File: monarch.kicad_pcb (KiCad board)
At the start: 2 copper layers, 159.6 x 123.3 mm, 141 parts, among them J1 USB_C_Receptacle_USB2.0, J2 USB_C_Receptacle_USB2.0, J3 OLED, SW1 SW_PUSH, SW10 SW_PUSH, SW11 SW_PUSH, SW12 SW_PUSH, SW13 SW_PUSH, SW14 SW_PUSH, SW15 SW_PUSH, SW16 SW_PUSH, SW17 SW_PUSH, SW18 SW_PUSH, SW19 Rotary_Encoder, SW2 SW_PUSH, SW20 SW_PUSH, SW21 SW_PUSH, SW22 SW_PUSH, SW23 SW_PUSH, SW24 SW_PUSH, SW3 SW_PUSH, SW4 SW_PUSH, SW5 SW_PUSH, SW6 SW_PUSH, SW7 SW_PUSH, SW8 SW_PUSH, SW9 SW_PUSH, U1 ATMEGA32U4, U2 MIC5219-5.0YMM, X1 16Mhz

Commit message: start routing
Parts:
- removed R10, R9: 330, Resistor_SMD:R_0805_2012Metric
- removed R11, R12: 5.1k, Resistor_SMD:R_0805_2012Metric
- J1, J2: footprint private:USB_C_TH_6pin -> Connector_USB:USB_C_Receptacle_GCT_USB4085; moved to B.Cu
- L1, L2: moved to F.Cu
- moved L1 169.7 mm to (181.0, 86.5), turned to 80 degrees
- moved L2 151.8 mm to (171.1, 84.1), turned to 80 degrees
- moved L34 143.7 mm to (18.3, 72.0)
- moved C3 139.2 mm to (21.0, 30.0)
- moved JP1 132.7 mm to (32.9, 22.6)
- moved L35 120.1 mm to (19.1, 30.6)
- moved L3 110.5 mm to (138.7, 18.9)
- moved L33 109.5 mm to (59.3, 96.0)
- moved R4 109.4 mm to (39.0, 14.7), turned to 0 degrees
- moved R3 108.5 mm to (39.0, 12.6), turned to 0 degrees
- moved R1 96.4 mm to (144.2, 19.6)
- moved L15 95.3 mm to (119.2, 49.0), turned to 0 degrees
- moved L20 95.3 mm to (24.2, 56.8), turned to 0 degrees
- moved L4 80.1 mm to (155.2, 46.1)
- moved L8 64.8 mm to (119.4, 117.2)
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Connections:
- R3 pad 1: +5V -> GND
- R4 pad 1: +5V -> GND
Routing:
- net VCC: track 0.00 -> 468.2 mm, vias 0 -> 2
- net A5: track 0.00 -> 185.9 mm
- net A2: track 0.00 -> 129.7 mm
- net A1: track 0.00 -> 113.2 mm
- net A3: track 0.00 -> 110.8 mm
- net A4: track 0.00 -> 109.1 mm, vias 0 -> 2
- net A0: track 0.00 -> 99.9 mm
- net Net-(BZ1-Pad1): track 0.00 -> 88.3 mm, vias 0 -> 2
- net Net-(L33-Pad3): track 0.00 -> 72.7 mm
- net Net-(L33-Pad1): track 0.00 -> 53.5 mm, vias 0 -> 2
- net COL0: track 38.4 -> 91.7 mm
- net Net-(L34-Pad1): track 0.00 -> 47.4 mm
- net Net-(D27-Pad1): track 0.00 -> 47.4 mm
- net COL1: track 38.0 -> 85.0 mm, vias 0 -> 4
- net RX: track 0.00 -> 39.4 mm
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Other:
- net class Default: via_dia 0.8 -> 0.6; via_drill 0.4 -> 0.3

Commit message: plate edge case
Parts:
- removed the H9 at (165.0, 126.7)
- removed the H9 at (147.8, 91.7)
- added H1: Hole, MountingHole:MountingHole_2.2mm_M2, F.Cu at (132.0, 14.2)
- added H1: Hole, MountingHole:MountingHole_2.2mm_M2, F.Cu at (155.6, 20.4)
- added H1: Hole, MountingHole:MountingHole_2.2mm_M2, F.Cu at (111.0, 120.7)
- added H1: Hole, MountingHole:MountingHole_2.2mm_M2, F.Cu at (14.9, 90.9)
- added H1: Hole, MountingHole:MountingHole_2.2mm_M2, F.Cu at (15.6, 15.1)
- added H1: Hole, MountingHole:MountingHole_2.2mm_M2, F.Cu at (77.8, 8.11)
- added H9: Hole, MountingHole:MountingHole_2.2mm_M2, F.Cu at (167.4, 130.7)
- moved L1 103.0 mm to (78.6, 75.6), turned to 0 degrees
- moved L2 84.9 mm to (86.7, 75.7), turned to 0 degrees
- moved R3 15.6 mm to (26.5, 21.9), turned to 90 degrees
- moved H10 12.4 mm to (81.2, 102.2)
- moved R4 5.89 mm to (33.4, 13.1), turned to 270 degrees
- moved L7 4.63 mm to (154.4, 121.6), turned to 350 degrees
- moved RED1 3.13 mm to (149.6, 23.4)
- moved L3 2.41 mm to (138.9, 16.6)
- moved L8 2.20 mm to (120.7, 115.4), turned to 350 degrees
- moved L43 2.00 mm to (122.0, 19.5)
- moved D26 1.88 mm to (134.6, 23.4)
- moved J2 1.07 mm to (163.5, 97.5)
- moved L42 1.00 mm to (109.8, 16.5)
- moved H2 0.94 mm to (155.6, 86.2)
- moved H4 0.60 mm to (132.0, 82.2)
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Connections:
- D1 pad 1: A3 -> A2
- D10 pad 1: A2 -> A3
- D11 pad 1: A2 -> A3
- D12 pad 1: A2 -> A3
- D2 pad 1: A3 -> A2
- D3 pad 1: A3 -> A2
- D4 pad 1: A3 -> A2
- D5 pad 1: A3 -> A2
- D6 pad 1: A3 -> A2
- D7 pad 1: A2 -> A3
- D8 pad 1: A2 -> A3
- D9 pad 1: A2 -> A3
- J2 pad A5: +5V -> GND
- J2 pad B5: +5V -> GND
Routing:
- net A5: track 185.9 -> 0.00 mm
- net Net-(J1-PadA6): track 0.00 -> 147.7 mm, vias 0 -> 1
- net Net-(J1-PadA7): track 0.00 -> 142.3 mm, vias 0 -> 1
- net COL2: track 95.3 -> 229.6 mm, vias 6 -> 9
- net COL0: track 91.7 -> 196.7 mm, vias 0 -> 3
- net VCC: track 468.2 -> 372.8 mm
- net COL1: track 85.0 -> 169.1 mm, vias 4 -> 7
- net Net-(L33-Pad3): track 72.7 -> 0.00 mm
- net COL4: track 103.7 -> 172.4 mm, vias 4 -> 5
- net Net-(L7-Pad1): track 38.6 -> 0.00 mm
- net Net-(L3-Pad1): track 34.9 -> 0.00 mm
- net GND: track 0.00 -> 22.1 mm
- net Net-(L6-Pad1): track 21.5 -> 0.00 mm
- net A1: track 113.2 -> 133.0 mm, vias 0 -> 2
- net A3: track 110.8 -> 129.4 mm, vias 0 -> 2
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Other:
- board size 159.6 x 123.3 mm -> 165.4 x 129.6 mm

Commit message: routing almost complete
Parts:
- moved L1 73.2 mm to (117.2, 13.4)
- moved L2 73.2 mm to (125.3, 13.5)
- moved R8 26.1 mm to (156.7, 64.5)
- moved R7 2.90 mm to (131.5, 67.9)
- moved C5 2.30 mm to (131.5, 71.5)
- moved R5 1.70 mm to (131.5, 65.4)
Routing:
- net VCC: track 372.8 -> 934.1 mm, vias 2 -> 6
- net UVCC: track 29.6 -> 193.7 mm, vias 0 -> 2
- net D10: track 0.00 -> 160.3 mm, vias 0 -> 1
- net COL3: track 38.0 -> 180.8 mm, vias 4 -> 5
- net A5: track 0.00 -> 105.3 mm, vias 0 -> 2
- net Net-(D26-Pad1): track 0.00 -> 70.1 mm
- net Net-(L33-Pad3): track 0.00 -> 66.6 mm
- net A0: track 101.6 -> 161.3 mm, vias 2 -> 4
- net GND: track 22.1 -> 76.8 mm, vias 3 -> 21
- net COL2: track 229.6 -> 176.2 mm
- net Net-(L26-Pad1): track 0.00 -> 51.9 mm, vias 0 -> 2
- net D2: track 0.00 -> 51.1 mm, vias 0 -> 1
- net D3: track 0.00 -> 49.3 mm, vias 0 -> 1
- net Net-(L3-Pad1): track 0.00 -> 42.6 mm
- net Net-(L7-Pad1): track 0.00 -> 31.8 mm
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
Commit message: rerouting v2
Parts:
- X1: footprint Crystal:Crystal_SMD_SeikoEpson_FA238-4Pin_3.2x2.5mm -> Crystal:Crystal_SMD_7050-4Pin_7.0x5.0mm
- moved R6 44.6 mm to (148.1, 18.0), turned to 180 degrees
- moved R3 8.26 mm to (23.9, 14.1), turned to 270 degrees
- moved R4 7.00 mm to (26.4, 14.0)
- moved C4 2.25 mm to (147.7, 79.2), turned to 135 degrees
- moved C2 1.53 mm to (155.5, 71.3), turned to 135 degrees
- moved X1 0.58 mm to (151.7, 75.3), turned to 45 degrees
- moved L1 0.29 mm to (117.2, 13.2)
- moved L2 0.29 mm to (125.3, 13.2)
- moved J2 0.05 mm to (163.4, 97.5)
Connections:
- X1 pad 3: (no net) -> GND
- X1 pad 4: (no net) -> GND
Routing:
- net GND: track 76.8 -> 153.7 mm, vias 21 -> 22
- net D9: track 0.00 -> 62.3 mm
- net VCC: track 934.1 -> 994.2 mm, vias 6 -> 21
- net Net-(R6-Pad1): track 4.15 -> 51.9 mm, vias 0 -> 2
- net COL4: track 174.8 -> 219.9 mm, vias 5 -> 13
- net Net-(D27-Pad1): track 48.0 -> 11.9 mm
- net A1: track 163.2 -> 130.9 mm, vias 4 -> 2
- net Net-(Boot1-Pad1): track 0.00 -> 29.3 mm, vias 0 -> 2
- net COL1: track 179.1 -> 206.6 mm, vias 7 -> 13
- net COL0: track 199.2 -> 225.6 mm, vias 0 -> 4
- net A4: track 103.9 -> 126.5 mm, vias 2 -> 4
- net COL2: track 176.2 -> 198.7 mm
- net Net-(L2-Pad1): track 0.00 -> 20.0 mm, vias 0 -> 1
- net Net-(D26-Pad1): track 70.1 -> 50.9 mm, vias 0 -> 1
- net A0: track 161.3 -> 142.7 mm, vias 4 -> 0
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
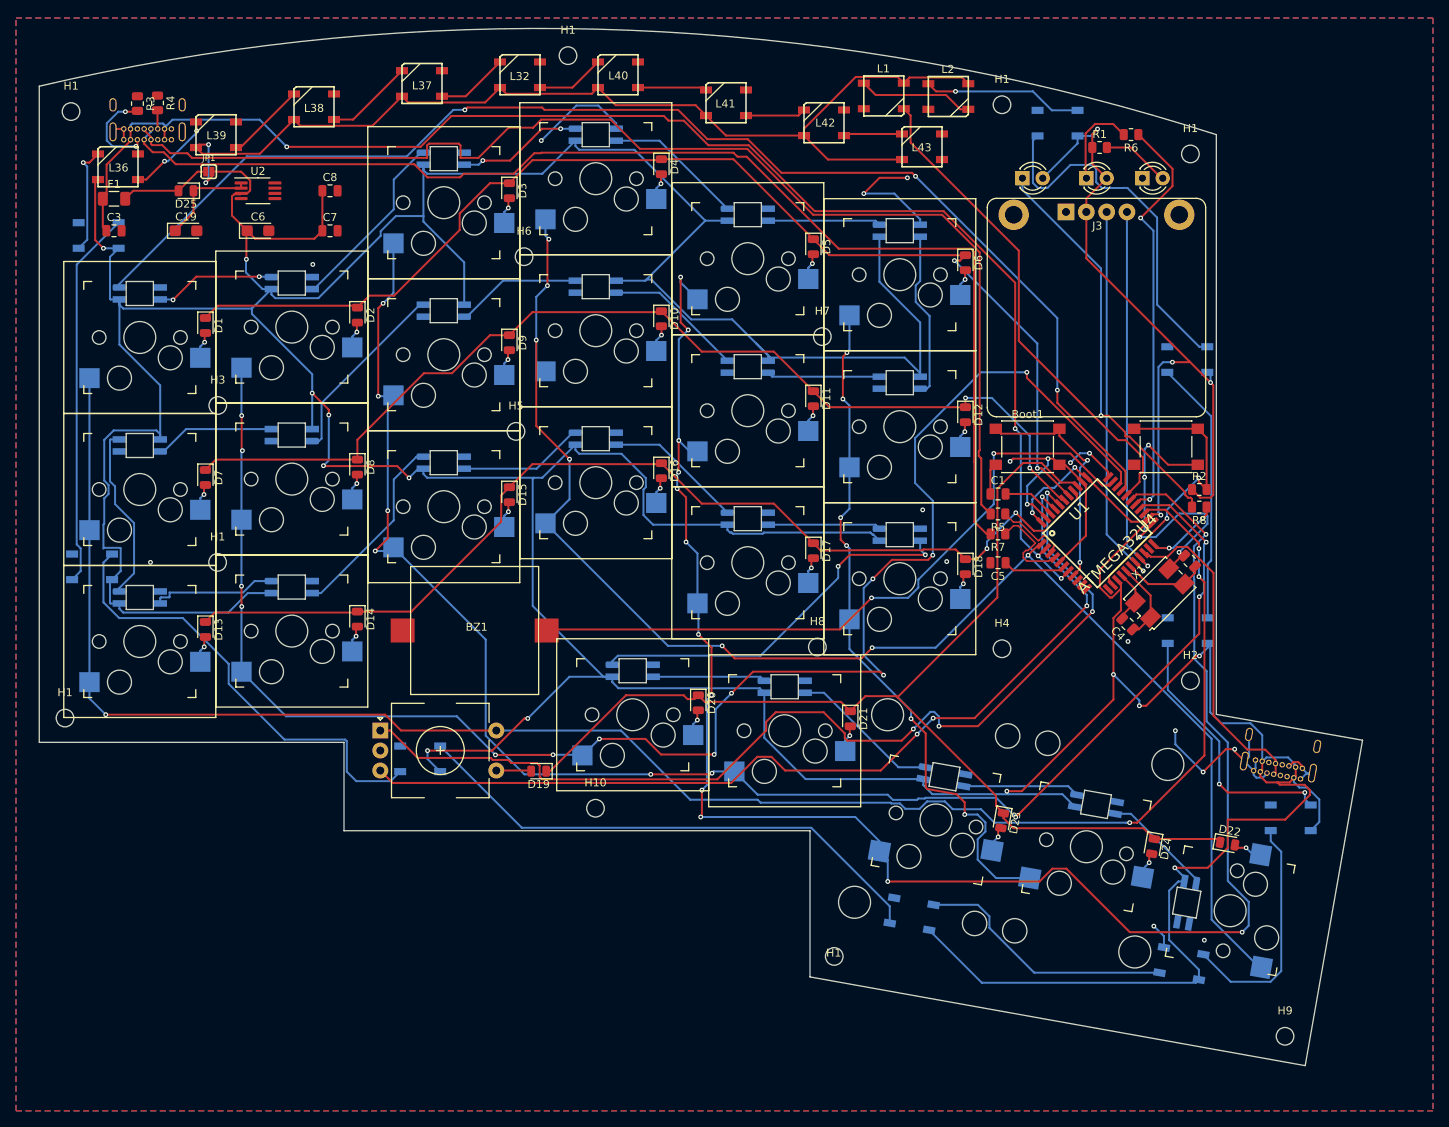
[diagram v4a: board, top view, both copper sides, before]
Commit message: rerouting 0 unrouted
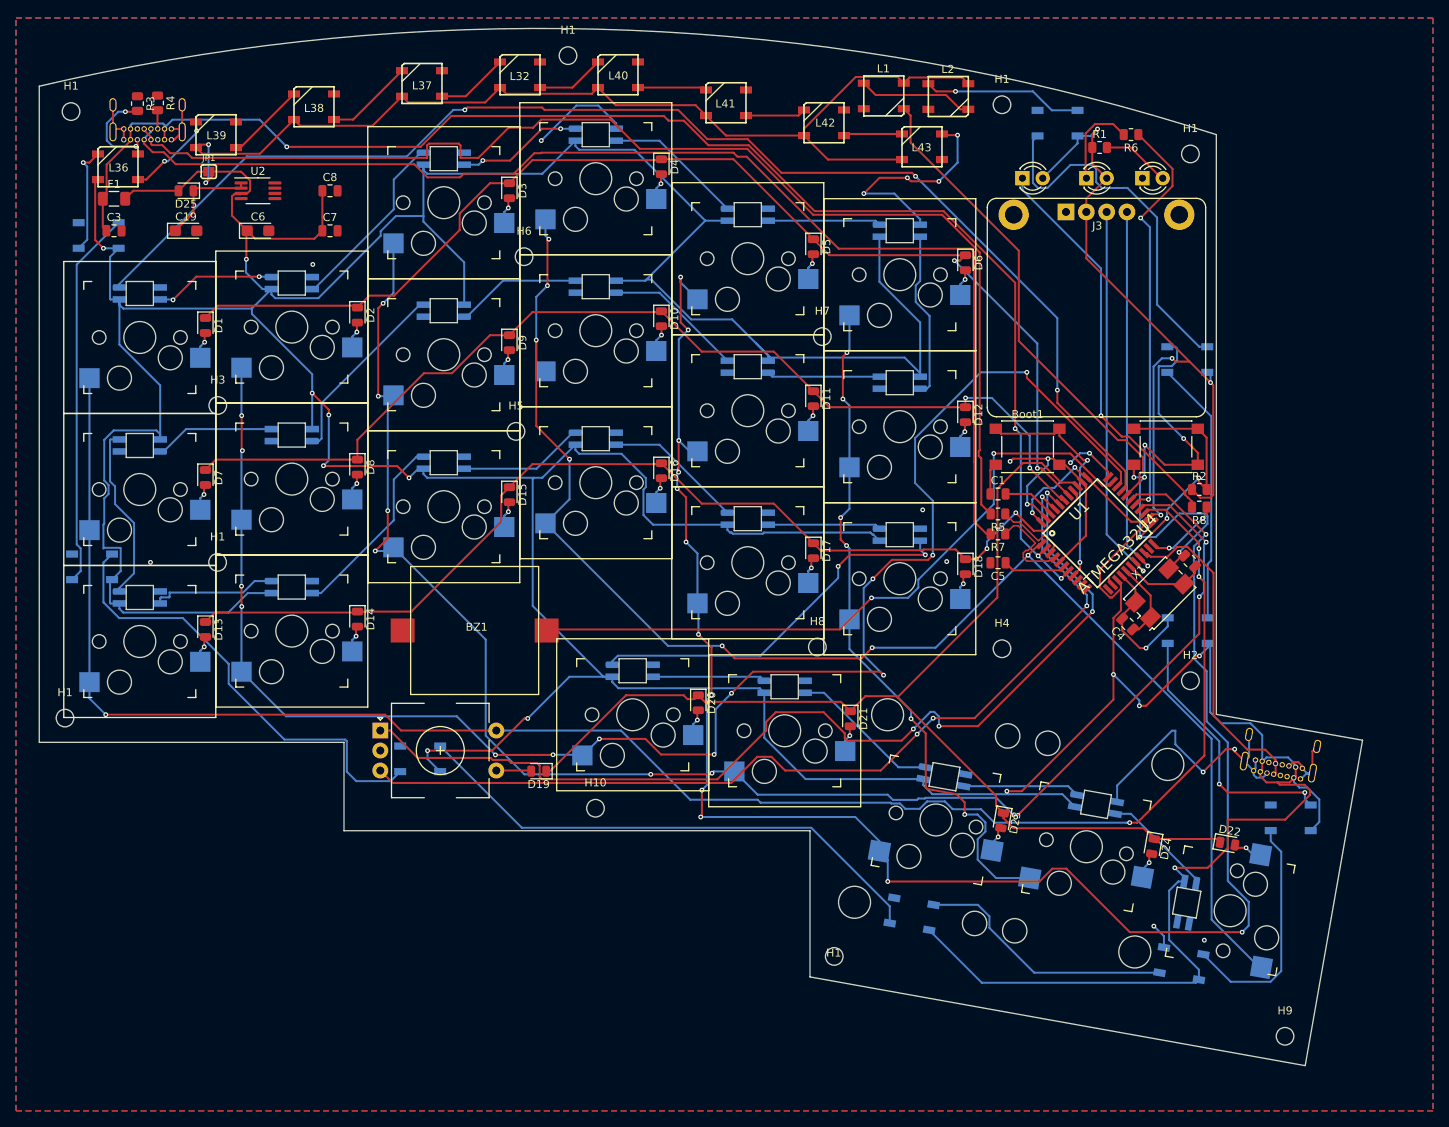
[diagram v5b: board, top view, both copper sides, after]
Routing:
- net GND: track 153.7 -> 225.6 mm, vias 22 -> 25
- net VCC: track 994.2 -> 995.5 mm

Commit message: pre tht crystal
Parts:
- added 16mhz1: Crystal, Crystal:Crystal_HC49-4H_Vertical, F.Cu at (165.8, 81.5)
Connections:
- U1 pad 16: Net-(C4-Pad1) -> Net-(16mhz1-Pad1)
- U1 pad 17: Net-(C2-Pad1) -> Net-(16mhz1-Pad2)
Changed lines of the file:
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@@
     (tracks 1510)
     (zones 0)
-    (modules 142)
-    (nets 120)
+    (modules 143)
+    (nets 122)
   )
   (page A4)
@@
   (net 118 "Net-(J1-PadB8)")
   (net 119 "Net-(J1-PadA8)")
+  (net 120 "Net-(16mhz1-Pad2)")
+  (net 121 "Net-(16mhz1-Pad1)")
   (net_class Default "This is the default net class."
     (clearance 0.2)
@@
     (add_net MISO)
     (add_net MOSI)
+    (add_net "Net-(16mhz1-Pad1)")
+    (add_net "Net-(16mhz1-Pad2)")
     (add_net "Net-(BZ1-Pad1)")
     (add_net "Net-(Boot1-Pad1)")
@@
     (uvia_drill 0.1)
   )
+  (module Crystal:Crystal_HC49-4H_Vertical (layer F.Cu)
+    (at 165.83 81.53 45)
+    (descr "Crystal THT HC-49-4H http://5hertz.com/pdfs/04404_D.pdf")
+    (tags "THT crystalHC-49-4H")
+    (fp_text reference 16mhz1 (at 2.44 -3.525 45) (layer F.SilkS)
+      (effects (font (size 1 1) (thickness 0.15)))
+    )
+    (fp_text value Crystal (at 2.44 3.525 45) (layer F.Fab)
+      (effects (font (size 1 1) (thickness 0.15)))
+    )
+    (fp_arc (start 5.64 0) (end 5.64 -2.525) (angle 180) (layer F.SilkS) (width 0.12))
+    (fp_arc (start -0.76 0) (end -0.76 -2.525) (angle -180) (layer F.SilkS) (width 0.12))
+    (fp_arc (start 5.44 0) (end 5.44 -2) (angle 180) (layer F.Fab) (width 0.1))
+    (fp_arc (start -0.56 0) (end -0.56 -2) (angle -180) (layer F.Fab) (width 0.1))
+    (fp_arc (start 5.64 0) (end 5.64 -2.325) (angle 180) (layer F.Fab) (width 0.1))
+    (fp_arc (start -0.76 0) (end -0.76 -2.325) (angle -180) (layer F.Fab) (width 0.1))
+    (fp_text user %R (at 2.44 0 45) (layer F.Fab)
+      (effects (font (size 1 1) (thickness 0.15)))
+    )
+    (fp_line (start -0.76 -2.325) (end 5.64 -2.325) (layer F.Fab) (width 0.1))
+    (fp_line (start -0.76 2.325) (end 5.64 2.325) (layer F.Fab) (width 0.1))
+    (fp_line (start -0.56 -2) (end 5.44 -2) (layer F.Fab) (width 0.1))
+    (fp_line (start -0.56 2) (end 5.44 2) (layer F.Fab) (width 0.1))
+    (fp_line (start -0.76 -2.525) (end 5.64 -2.525) (layer F.SilkS) (width 0.12))
+    (fp_line (start -0.76 2.525) (end 5.64 2.525) (layer F.SilkS) (width 0.12))
+    (fp_line (start -3.6 -2.8) (end -3.6 2.8) (layer F.CrtYd) (width 0.05))
+    (fp_line (start -3.6 2.8) (end 8.5 2.8) (layer F.CrtYd) (width 0.05))
+    (fp_line (start 8.5 2.8) (end 8.5 -2.8) (layer F.CrtYd) (width 0.05))
+    (fp_line (start 8.5 -2.8) (end -3.6 -2.8) (layer F.CrtYd) (width 0.05))
+    (pad 2 thru_hole circle (at 4.88 0 45) (size 1.5 1.5) (drill 0.8) (layers *.Cu *.Mask)
+      (net 120 "Net-(16mhz1-Pad2)"))
+    (pad 1 thru_hole circle (at 0 0 45) (size 1.5 1.5) (drill 0.8) (layers *.Cu *.Mask)
+      (net 121 "Net-(16mhz1-Pad1)"))
+    (model ${KISYS3DMOD}/Crystal.3dshapes/Crystal_HC49-4H_Vertical.wrl
+      (at (xyz 0 0 0))
+      (scale (xyz 1 1 1))
+      (rotate (xyz 0 0 0))
+    )
+  )
   (module Display:Generic_0.96in-128x64-OLED-Display-IIC (layer F.Cu)
     (at 143.81 39.6)
@@
       (net 94 GND) (solder_mask_margin 0.2))
     (pad 16 smd rect (at -0.8 5.9 45) (size 0.5 1.5) (layers F.Cu F.Paste F.Mask)
-      (net 69 "Net-(C4-Pad1)") (solder_mask_margin 0.2))
+      (net 121 "Net-(16mhz1-Pad1)") (solder_mask_margin 0.2))
     (pad 17 smd rect (at 0 5.9 45) (size 0.5 1.5) (layers F.Cu F.Paste F.Mask)
-      (net 68 "Net-(C2-Pad1)") (solder_mask_margin 0.2))
+      (net 120 "Net-(16mhz1-Pad2)") (solder_mask_margin 0.2))
     (pad 18 smd rect (at 0.8 5.9 45) (size 0.5 1.5) (layers F.Cu F.Paste F.Mask)
       (net 81 D3) (solder_mask_margin 0.2))

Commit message: final routing v2
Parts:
- removed C2, C4: 22pF, Capacitor_SMD:C_0805_2012Metric
- removed the H1 at (15.6, 15.1)
- removed the H1 at (77.8, 8.11)
- removed X1: 16Mhz, Crystal:Crystal_SMD_7050-4Pin_7.0x5.0mm
- added H1: Hole, MountingHole:MountingHole_2.2mm_M2, F.Cu at (15.6, 14.4)
- added H1: Hole, MountingHole:MountingHole_2.2mm_M2, F.Cu at (77.7, 7.44)
- L1, L2: moved to B.Cu
- moved L1 71.2 mm to (46.0, 14.5)
- moved L2 27.8 mm to (97.5, 14.0)
- moved 16mhz1 16.5 mm to (149.8, 77.5)
- moved R4 1.35 mm to (27.1, 15.2), turned to 180 degrees
- moved R3 1.10 mm to (23.7, 15.2), turned to 180 degrees
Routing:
- net D9: track 62.3 -> 132.8 mm, vias 0 -> 1
- net Net-(L1-Pad1): track 14.4 -> 58.0 mm
- net Net-(L2-Pad1): track 20.0 -> 50.4 mm, vias 1 -> 2
- net GND: track 225.6 -> 198.4 mm
- net VCC: track 995.5 -> 980.5 mm, vias 21 -> 23
- net UVCC: track 181.7 -> 193.9 mm
- net Net-(C2-Pad1): track 10.3 -> 0.00 mm
- net Net-(C4-Pad1): track 9.88 -> 0.00 mm
- net Net-(16mhz1-Pad2): track 0.00 -> 6.01 mm
- net Net-(16mhz1-Pad1): track 0.00 -> 5.87 mm
- net Net-(J1-PadA5): track 11.5 -> 10.7 mm
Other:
- board text added: "butterfly rev1.0"
- board text removed: "monarch rev1.0"
